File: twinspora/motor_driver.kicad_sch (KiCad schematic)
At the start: 17 parts, among them U6 DRV8316CRRGFR

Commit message: initial completion
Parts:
- added J14: Conn_01x03, Connector_DORABO:CONN-TH_DB125-2.54-3P-GN, symbol Connector_Generic:Conn_01x03
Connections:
- net PHA: now also J14.1 (Pin_1)
- net PHB: now also J14.2 (Pin_2)
- net PHC: now also J14.3 (Pin_3)
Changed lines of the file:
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@@
+		)
+	)
+	(hierarchical_label "PHC"
+		(shape input)
+		(at 210.82 90.17 180)
+		(effects
+			(font
+				(size 1.27 1.27)
+			)
+			(justify right)
 		)
 	)
@@
 		)
 	)
+	(hierarchical_label "PHB"
+		(shape input)
+		(at 210.82 87.63 180)
+		(effects
+			(font
+				(size 1.27 1.27)
+			)
+			(justify right)
+		)
+	)
 	(hierarchical_label "CH2N"
 		(shape input)
@@
 		(shape input)
 		(at 125.73 95.25 180)
+		(effects
+			(font
+				(size 1.27 1.27)
+			)
+			(justify right)
+		)
+	)
+	(hierarchical_label "PHA"
+		(shape input)
+		(at 210.82 85.09 180)
 		(effects
 			(font
@@
 					(unit 1)
 				)
+			)
+		)
+	)
+	(symbol
+		(lib_id "Connector_Generic:Conn_01x03")
+		(at 215.9 87.63 0)
+		(unit 1)
+		(body_style 1)
+		(exclude_from_sim no)
+		(in_bom yes)
+		(on_board yes)
+		(in_pos_files yes)
+		(dnp no)
+		(property "Reference" "J14"
+			(at 218.44 86.3599 0)
+			(show_name no)
+			(do_not_autoplace no)
+			(effects
+				(font
+					(size 1.27 1.27)
+				)
+				(justify left)
+			)
+		)
+		(property "Value" "Conn_01x03"
+			(at 218.44 88.8999 0)
+			(show_name no)
+			(do_not_autoplace no)
+			(effects
+				(font
+					(size 1.27 1.27)
+				)
+				(justify left)
+			)
+		)
+		(property "Footprint" "Connector_DORABO:CONN-TH_DB125-2.54-3P-GN"
+			(at 215.9 87.63 0)
+			(hide yes)
+			(show_name no)
+			(do_not_autoplace no)
+			(effects
+				(font
+					(size 1.27 1.27)
+				)
+			)
+		)
+		(property "Datasheet" ""
+			(at 215.9 87.63 0)
+			(hide yes)
+			(show_name no)
+			(do_not_autoplace no)
+			(effects
+				(font
+					(size 1.27 1.27)
+				)
+			)
+		)
+		(property "Description" "Generic connector, single row, 01x03, script generated (kicad-library-utils/schlib/autogen/connector/)"
+			(at 215.9 87.63 0)
+			(hide yes)
+			(show_name no)
+			(do_not_autoplace no)
+			(effects
+				(font
+					(size 1.27 1.27)
+				)
+			)
+		)
+		(pin "1"
+		)
+		(pin "3"
+		)
+		(pin "2"
+		)
+		(instances
+			(project ""
+				(path "/64e594d2-0aaa-4fb1-a4b5-254d61e53018/7d96679b-218a-4072-9a5c-233e6796257a"
+					(reference "J15")
+					(unit 1)
+				)
+				(path "/64e594d2-0aaa-4fb1-a4b5-254d61e53018/e10c8a45-fef0-4bcf-826b-88ad718f533d"
+					(reference "J14")
+					(unit 1)
+				)

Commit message: NEW
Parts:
- removed R20: 0402WGF5101TCE, Basic_Capacitors_Resistors:R0402, symbol Basic_Capacitors_Resistors:0402WGF5101TCE
- added C54: EEEFT1H331GP, Capacitor_SMD_UWRL:CAP-SMD_BD10.0-L10.3-W10.3-LS11.0-R-RD, symbol Capacitor_SMD_UWRL:EEEFT1H331GP
- added LED4: KT-0603R, LED:LED0603-RD, symbol LED:KT-0603R
- added R35: 0402WGF3300TCE, Resistor_SMD:R_0402_1005Metric, symbol Basic_Capacitors_Resistors:0402WGF3300TCE
- C27, C28, C36, C37, C38, C39, C40, C41: footprint Basic_Capacitors_Resistors:C0805 -> Capacitor_SMD:C_0805_2012Metric
- C35: footprint Basic_Capacitors_Resistors:C0402 -> Capacitor_SMD:C_0402_1005Metric
- D2: value BZT52B5V1S -> BZT52B5V1S_C19077434; footprint Diode:SOD-323_L1.7-W1.3-LS2.6-RD -> Diode_SMD:D_SOD-323_HandSoldering
- J14: footprint Connector_DORABO:CONN-TH_DB125-2.54-3P-GN -> (none)
- R19: footprint Basic_Capacitors_Resistors:R0402 -> Resistor_SMD:R_0402_1005Metric
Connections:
- net +3.3V: now also LED4.2 (A)
- net GND: now also C54.1
- net VCC: now also C54.2
- net VCP: now reaches C26.2, U6.8 (CP)
- net nFAULT: now reaches U6.22 (nFAULT)
- net nFAULT: now also R35.2
- new net: LED4.1 (K), R35.1
- no-connect marks 3 -> 4
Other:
- moved on the sheet: D2, R19

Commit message: fix shit
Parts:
- C20, C25, C26: footprint Basic_Capacitors_Resistors:C0603 -> Capacitor_SMD:C_0603_1608Metric
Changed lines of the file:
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@@
 		(dnp no)
 		(fields_autoplaced yes)
-		(property "Reference" "#PWR091"
+		(property "Reference" "#PWR91"
 			(at 109.22 87.63 0)
 			(hide yes)
@@
 			(project "twinspora"
 				(path "/64e594d2-0aaa-4fb1-a4b5-254d61e53018/7d96679b-218a-4072-9a5c-233e6796257a"
-					(reference "#PWR092")
-					(unit 1)
-				)
-				(path "/64e594d2-0aaa-4fb1-a4b5-254d61e53018/e10c8a45-fef0-4bcf-826b-88ad718f533d"
-					(reference "#PWR091")
+					(reference "#PWR92")
+					(unit 1)
+				)
+				(path "/64e594d2-0aaa-4fb1-a4b5-254d61e53018/e10c8a45-fef0-4bcf-826b-88ad718f533d"
+					(reference "#PWR91")
 					(unit 1)
 				)
@@
 			)
 		)
-		(property "Footprint" "Basic_Capacitors_Resistors:C0603"
+		(property "Footprint" "Capacitor_SMD:C_0603_1608Metric"
 			(at 138.43 72.39 0)
 			(hide yes)
@@
 		(fields_autoplaced yes)
 		(property "Reference" "C20"
-			(at 124.46 118.11 90)
-			(show_name no)
-			(do_not_autoplace no)
-			(effects
-				(font
-					(size 1.27 1.27)
-				)
-				(justify left)
+			(at 124.46 118.1099 90)
+			(show_name no)
+			(do_not_autoplace no)
+			(effects
+				(font
+					(size 1.27 1.27)
+				)
+				(justify right)
 			)
 		)
@@
 			)
 		)
-		(property "Footprint" "Basic_Capacitors_Resistors:C0603"
+		(property "Footprint" "Capacitor_SMD:C_0603_1608Metric"
 			(at 130.81 118.11 0)
 			(hide yes)
@@
 			)
 		)
-		(property "Footprint" "Basic_Capacitors_Resistors:C0603"
+		(property "Footprint" "Capacitor_SMD:C_0603_1608Metric"
 			(at 151.13 72.39 0)
 			(hide yes)
@@
 		(fields_autoplaced yes)
 		(property "Reference" "LED4"
-			(at 100.33 91.44 0)
-			(show_name no)
-			(do_not_autoplace no)
-			(effects
-				(font
-					(size 1.27 1.27)
-				)
+			(at 113.03 90.1699 90)
+			(show_name no)
+			(do_not_autoplace no)
+			(effects
+				(font
+					(size 1.27 1.27)
+				)
+				(justify right)
 			)
 		)
 		(property "Value" "KT-0603R"
-			(at 102.87 91.44 0)
-			(show_name no)
-			(do_not_autoplace no)
-			(effects
-				(font
-					(size 1.27 1.27)
-				)
+			(at 113.03 92.7099 90)
+			(show_name no)
+			(do_not_autoplace no)
+			(effects
+				(font
+					(size 1.27 1.27)
+				)
+				(justify right)
 			)
 		)
@@
 		(fields_autoplaced yes)
 		(property "Reference" "R35"
-			(at 104.14 101.6 0)
-			(show_name no)
-			(do_not_autoplace no)
-			(effects
-				(font
-					(size 1.27 1.27)
-				)
-			)
-		)
+			(at 111.76 101.5999 90)
+			(show_name no)
+			(do_not_autoplace no)
+			(effects
+				(font
+					(size 1.27 1.27)
+				)
+				(justify right)
+			)
+		)

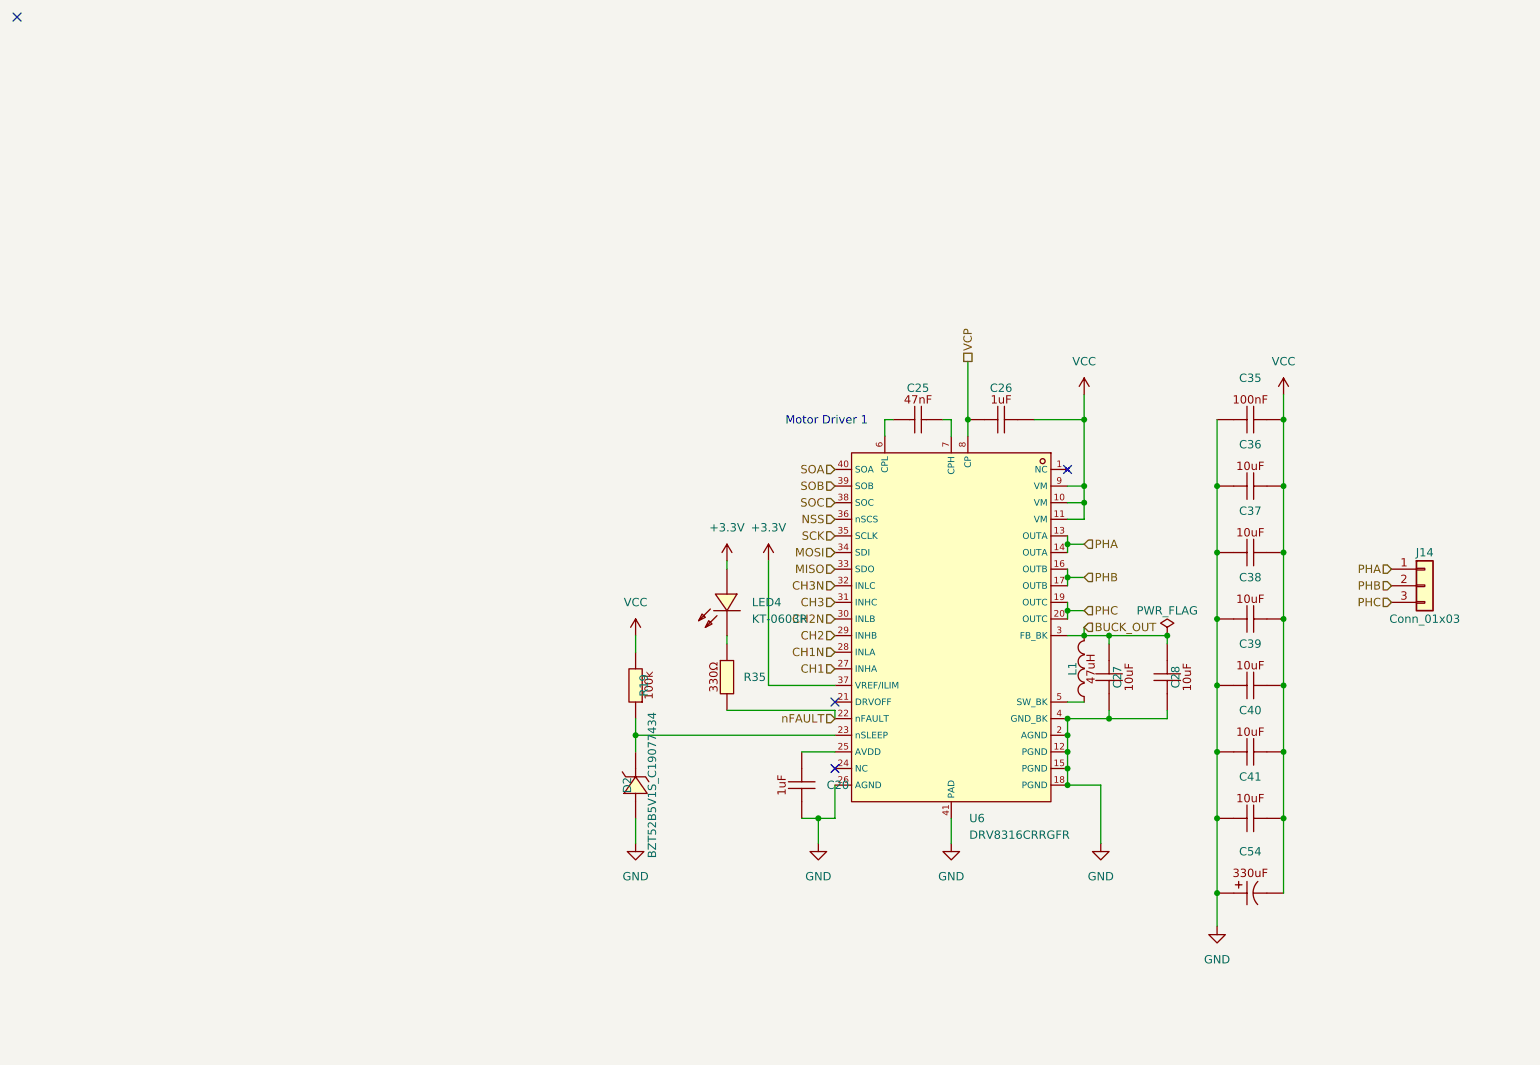
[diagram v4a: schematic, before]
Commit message: split terminatino for can
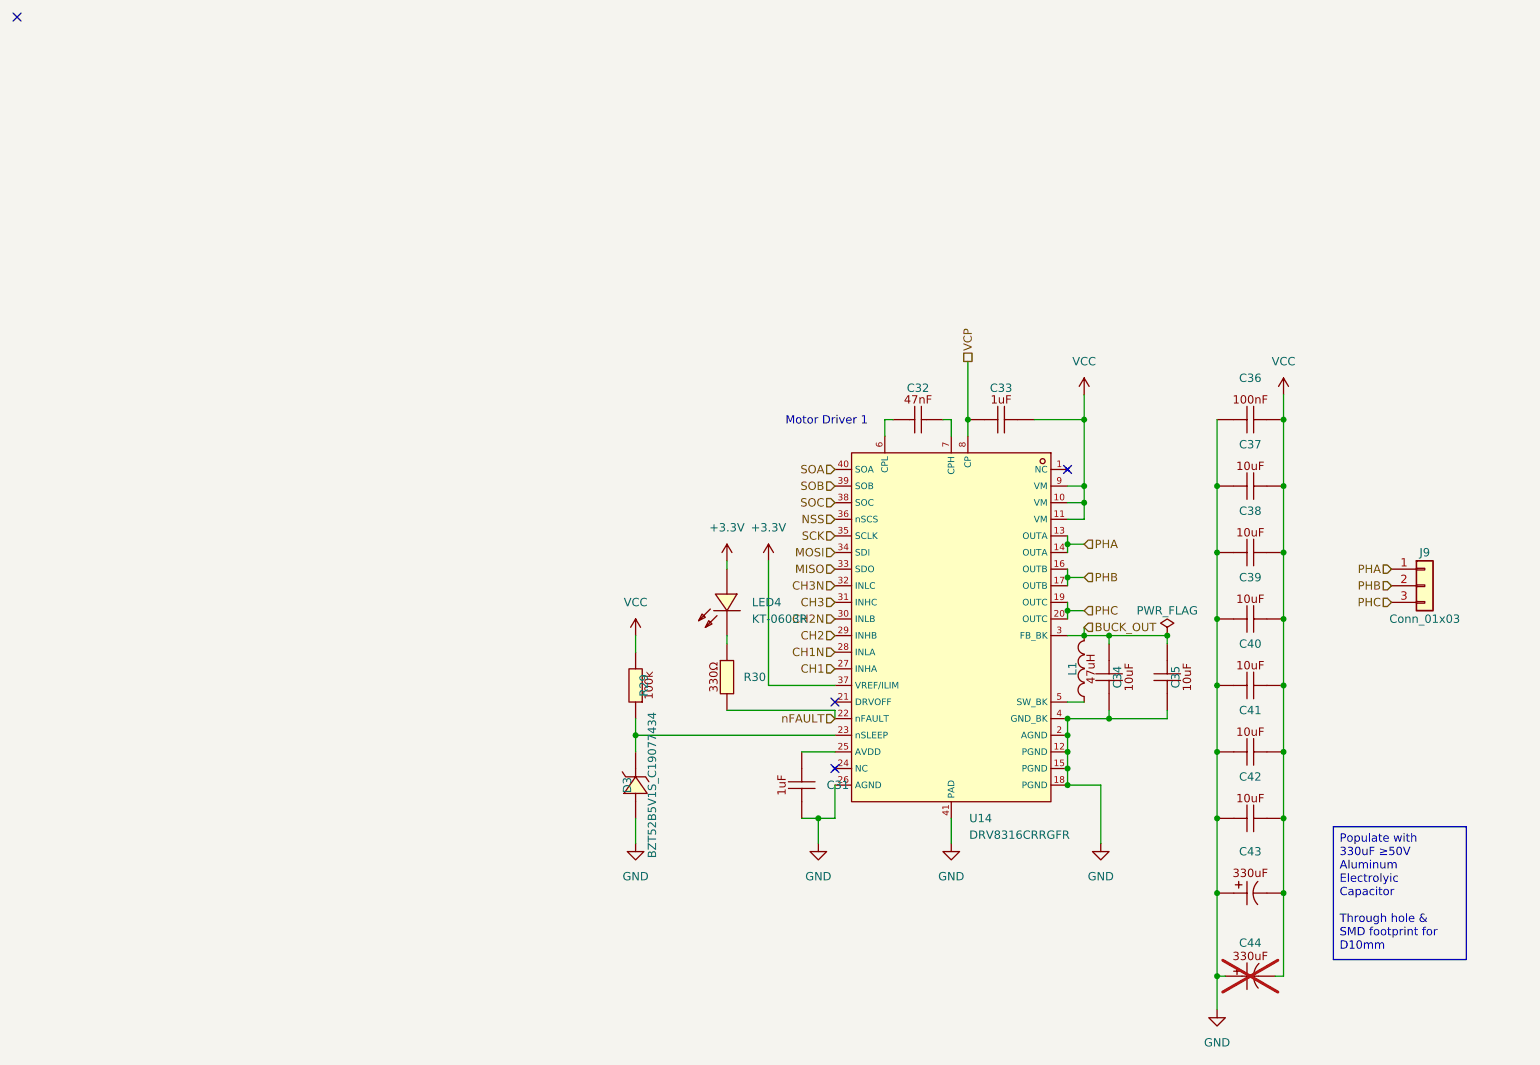
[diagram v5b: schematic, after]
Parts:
- added C44: 50PX330MEFC10X16, Capacitor_THT_UWRL:CAP-TH_BD10.0-P5.00-D1.0-FD, symbol Capacitor_THT_UWRL:50PX330MEFC10X16
- renumbered C20 to C31, C25 to C32, C26 to C33, C27 to C34, C28 to C35, C35 to C36, C36 to C37, C37 to C38, C38 to C39, C39 to C40, C40 to C41, C41 to C42, C54 to C43, D2 to D3, J14 to J9, R19 to R29, R35 to R30, U6 to U14
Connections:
- net GND: now also C44.1
- net VCC: now also C44.2

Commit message: rear silkscreen
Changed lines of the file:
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@@
 		)
 	)
-	(text_box "Populate with 330uF ≥50V \nAluminum Electrolyic Capacitor\n\nThrough hole & SMD footprint for D10mm"
+	(text_box "Populate with 330uF ≥50V \nAluminum Electrolyic Capacitor\n\nThrough hole & SMD footprint for 10mm diameter\n\nThrough hole recommended for better mechanical strength"
 		(exclude_from_sim no)
-		(at 201.93 124.4747 0)
-		(size 20.32 20.3053)
+		(at 199.39 120.65 0)
+		(size 20.32 30.5285)
 		(margins 0.9525 0.9525 0.9525 0.9525)
 		(stroke
 			(width 0)
-			(type solid)
+			(type dot)
 		)
 		(fill
